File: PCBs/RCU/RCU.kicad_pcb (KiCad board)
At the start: 4 copper layers, 99 x 139 mm, 148 parts, among them J100 Conn_01x02, J200 USB_C_Receptacle_USB2.0, J201 Conn_01x05, J300 Right_Motor_Screw_Terminal, J301 Right_Encoder_Conn, J302 Left_Motor_Screw_Terminal, J303 Left_Encoder_Conn, J400 USB_C_Receptacle_USB2.0, Q400 2N7002NXAKR (NMOS), Q401 2N7002NXAKR (NMOS), Q402 BSS84AK,215 (PMOS), Q403 2N7002NXAKR (NMOS), SW201 SW_Push, SW400 SW_Push, SW401 SW_SPDT, U100 LM2576S-ADJ, U101 AP63203WU, U102 AZ1117-3.3, U200 STM32G0B1CBT6, U201 USBLC6-2SC6, U300 OPA320, U301 DRV8876, U302 OPA320, U303 DRV8876, U400 USBLC6-2SC6, U401 CH340C, U402 ESP32-MINI-1, U403 DG2788ADN-T1-GE4, U500 APDS-9306-065, U501 LSM6DS3, U502 SHT30-DIS, U600 ADC121C027CIMK/NOPB, U601 OPA320, U602 ADC121C027CIMK/NOPB, U603 OPA320, U700 SST26VF032BT-104I/SM, Y200 16MHz

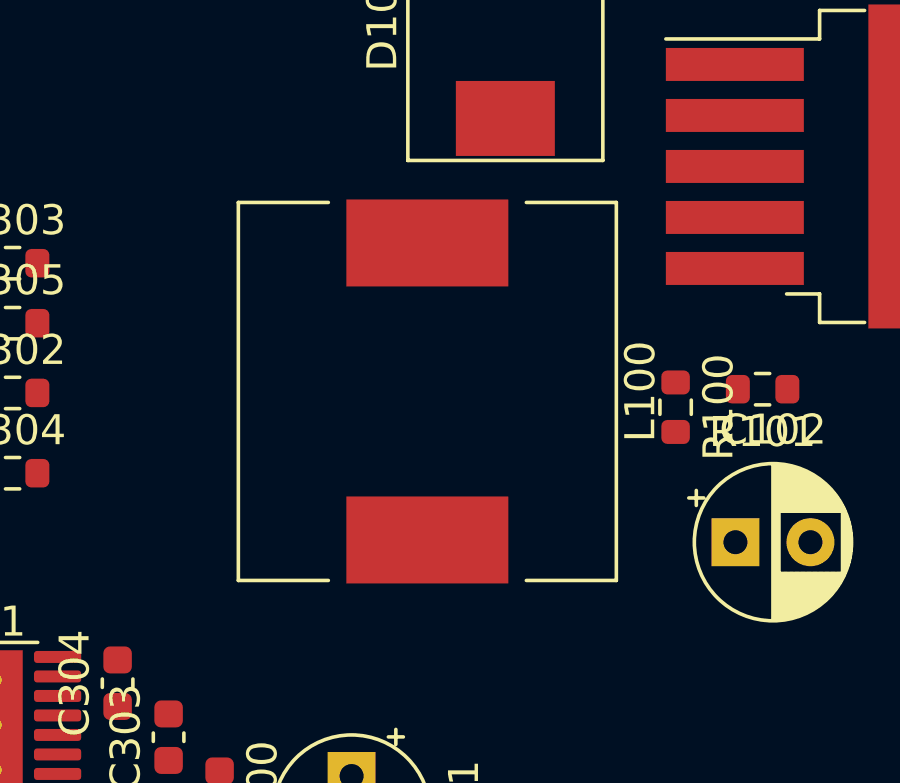
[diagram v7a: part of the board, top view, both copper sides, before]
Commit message: add MWSA1206S 68uH inductor footprint and 3d model
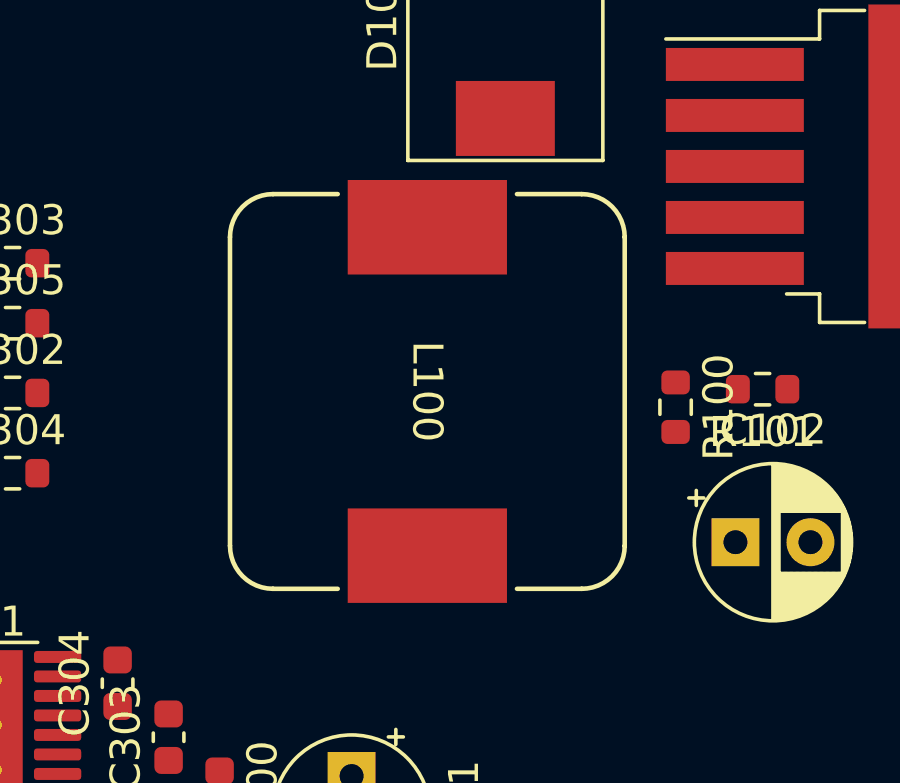
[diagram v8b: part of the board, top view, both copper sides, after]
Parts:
- L100: footprint Inductor_SMD:L_12x12mm_H6mm -> 68uH Power Inductor:IND_MWSA1206S_SNL
